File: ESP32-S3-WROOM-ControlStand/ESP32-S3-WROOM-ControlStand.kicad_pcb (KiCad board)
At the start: 2 copper layers, 198.1 x 126.4 mm, 167 parts, among them IC601 USBLC6-2SC6, J1 Button & LED Panel, J10 RJ45, J11 Barrel_Jack, J12 Battery, J2 Button & LED Panel, J3 STEMMA (Display), J4 Horn, J5 Brake, J6 Light Switch, J601 GCT_USB4105, J7 Reverser, J8 Throttle, J9 RJ45, P1 CONN_8, P2 Misc buttons, bell, status LED, P6 CONN_3, P7 CONN_3, P8 CONN_5, P9 CONN_5, SW1 A, SW10 SW_PUSH_SMALL, SW11 SW_PUSH_SMALL, SW12 SW_PUSH_SMALL, SW13 SW_PUSH_SMALL, SW14 SW_PUSH_SMALL, SW15 SW_PUSH_SMALL, SW16 SW_PUSH_SMALL, SW17 SW_PUSH_SMALL, SW18 SW_PUSH_SMALL, SW19 SW_PUSH_SMALL, SW2 B, SW20 SW_PUSH_SMALL, SW21 SW_PUSH_SMALL, SW22 SW_PUSH_SMALL, SW23 On/Off, SW24 RESET, SW3 C, SW4 D, SW5 Bell, SW601 BOOT, SW7 SW_PUSH_SMALL, SW8 SW_PUSH_SMALL, SW9 SW_PUSH_SMALL, T1 Buttons, T2 LEDS, T3 Buttons, T4 LEDS, T5 + 15 in -, T6 + 15 out -, U1 MCP23017, U2 TBD62083A, U3 MCP23017, U4 TBD62083A, U5 TCAN332DR, U6 MCP73871, U601 ESP32_S3_WROOM-1, U7 LM2574HVM-5.0, U8 TC1263-3.3VOATR

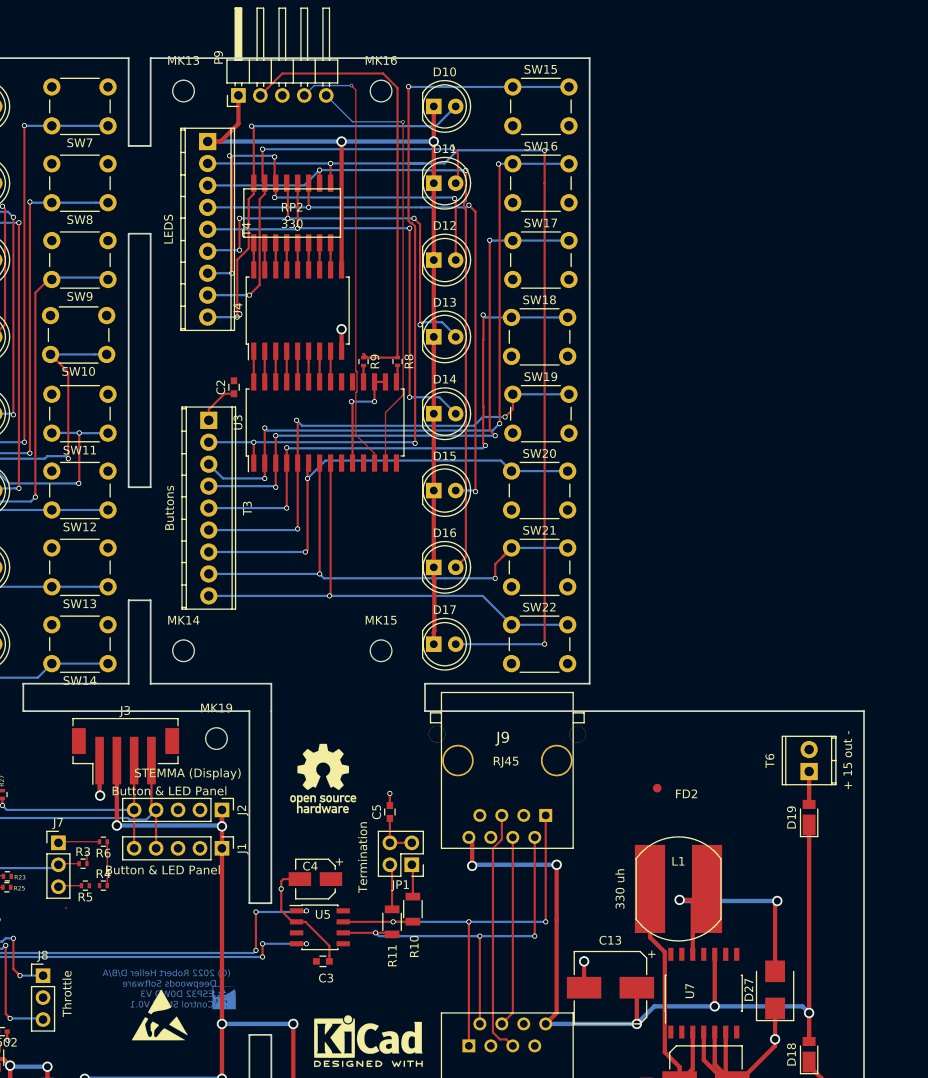
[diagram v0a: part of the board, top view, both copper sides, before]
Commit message: Add Keypad board.
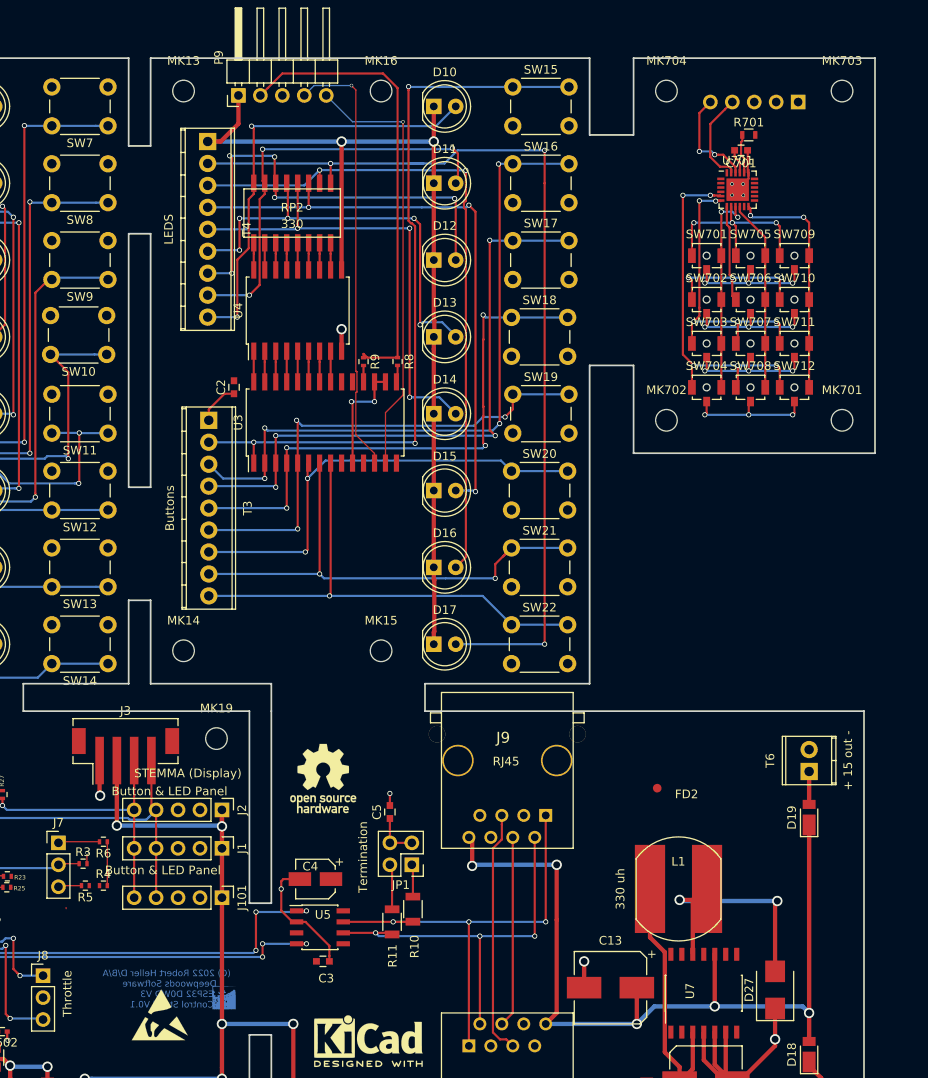
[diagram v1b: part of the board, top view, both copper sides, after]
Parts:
- added C701: .1uf, Capacitors_SMD:C_0603, F.Cu at (234.7, 36.1)
- added J101: Keypad Panel, Pin_Headers:Pin_Header_Straight_1x05_Pitch2.54mm, F.Cu at (174.6, 122.6)
- added MK701: Mounting_Hole, Mounting_Holes:MountingHole_2.5mm, F.Cu at (246.4, 67.3)
- added MK702: Mounting_Hole, Mounting_Holes:MountingHole_2.5mm, F.Cu at (226.1, 67.3)
- added MK703: Mounting_Hole, Mounting_Holes:MountingHole_2.5mm, F.Cu at (246.4, 29.2)
- added MK704: Mounting_Hole, Mounting_Holes:MountingHole_2.5mm, F.Cu at (226.1, 29.2)
- added P701: CONN_5, Pin_Headers:Pin_Header_Angled_1x05_Pitch2.54mm, B.Cu at (241.3, 30.5)
- added R701: 10K, Resistors_SMD:R_0603, F.Cu at (235.6, 34.3)
- added SW701: "1", Buttons_Switches_SMD:SW_SPST_B3U-1100P-B, F.Cu at (230.7, 49.1)
- added SW702: "4", Buttons_Switches_SMD:SW_SPST_B3U-1100P-B, F.Cu at (230.7, 54.2)
- added SW703: "7", Buttons_Switches_SMD:SW_SPST_B3U-1100P-B, F.Cu at (230.7, 59.2)
- added SW704: "*", Buttons_Switches_SMD:SW_SPST_B3U-1100P-B, F.Cu at (230.7, 64.3)
- added SW705: "2", Buttons_Switches_SMD:SW_SPST_B3U-1100P-B, F.Cu at (235.8, 49.1)
- added SW706: "5", Buttons_Switches_SMD:SW_SPST_B3U-1100P-B, F.Cu at (235.8, 54.2)
- added SW707: "8", Buttons_Switches_SMD:SW_SPST_B3U-1100P-B, F.Cu at (235.8, 59.2)
- added SW708: "0", Buttons_Switches_SMD:SW_SPST_B3U-1100P-B, F.Cu at (235.8, 64.3)
- added SW709: "3", Buttons_Switches_SMD:SW_SPST_B3U-1100P-B, F.Cu at (240.9, 49.1)
- added SW710: "6", Buttons_Switches_SMD:SW_SPST_B3U-1100P-B, F.Cu at (240.9, 54.2)
- added SW711: "9", Buttons_Switches_SMD:SW_SPST_B3U-1100P-B, F.Cu at (240.9, 59.2)
- added SW712: "#", Buttons_Switches_SMD:SW_SPST_B3U-1100P-B, F.Cu at (240.9, 64.3)
- added U701: TCA8418, Housings_DFN_QFN:QFN-24-1EP_4x4mm_Pitch0.5mm, F.Cu at (234.3, 40.6)
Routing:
- net GND: track 209.3 -> 279.0 mm, vias 40 -> 56
- net Net-(SW704-Pad1): track 0.00 -> 42.1 mm, vias 0 -> 5
- net Net-(SW703-Pad1): track 0.00 -> 34.3 mm, vias 0 -> 5
- net Net-(SW702-Pad1): track 0.00 -> 27.4 mm, vias 0 -> 3
- net Net-(SW709-Pad2): track 0.00 -> 27.3 mm, vias 0 -> 2
- net Net-(SW701-Pad2): track 0.00 -> 23.8 mm, vias 0 -> 2
- net Net-(SW701-Pad1): track 0.00 -> 23.3 mm, vias 0 -> 3
- net Net-(SW705-Pad2): track 0.00 -> 22.1 mm
- net /Keypad Panel/SDA: track 0.00 -> 11.8 mm, vias 0 -> 2
- net /Keypad Panel/SCL: track 0.00 -> 10.9 mm
- net /SDA: track 30.3 -> 36.0 mm
- net /SCL: track 64.6 -> 70.3 mm
- net Net-(R701-Pad1): track 0.00 -> 4.59 mm
- net +3V3: track 53.6 -> 56.4 mm
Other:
- board size 198.1 x 126.4 mm -> 199.4 x 126.4 mm
- net class Default: clearance 0.15 -> 0.1
- rule trace_clearance: 0.15 -> 0.1
